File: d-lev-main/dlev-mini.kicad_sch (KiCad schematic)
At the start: 5 parts

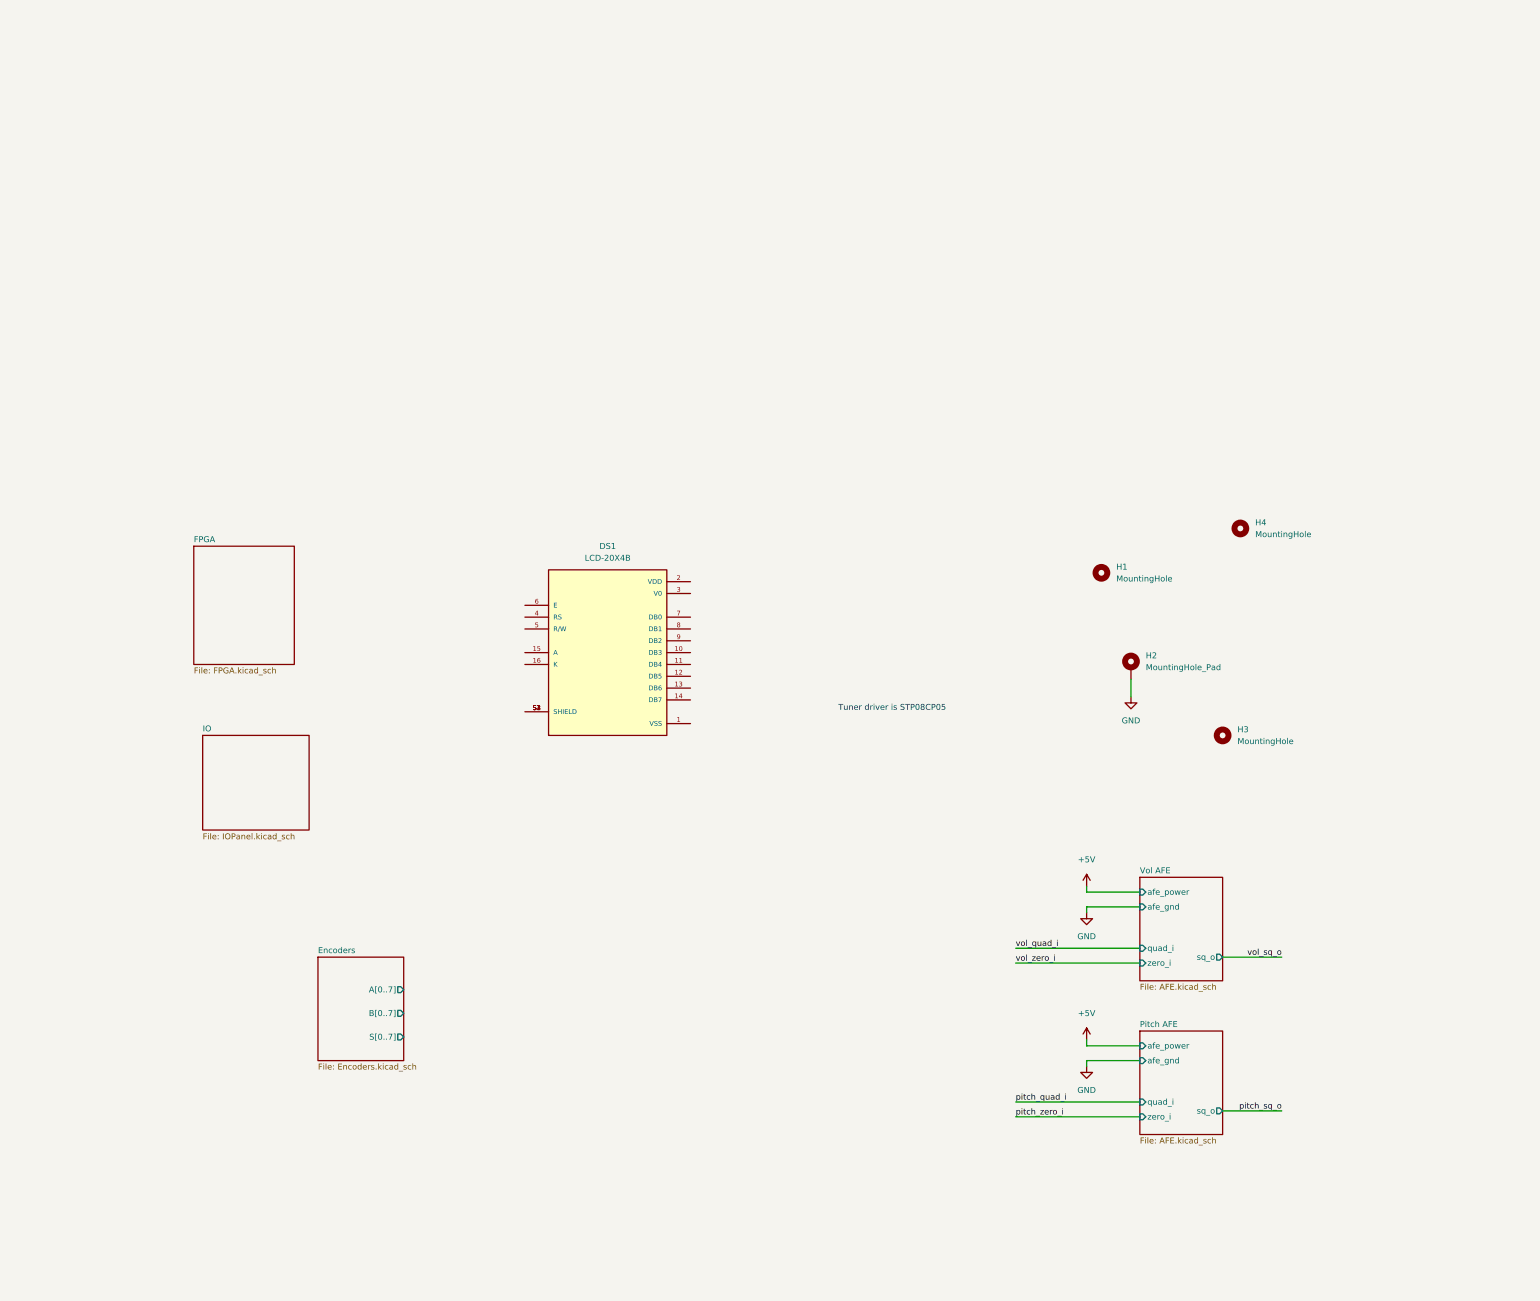
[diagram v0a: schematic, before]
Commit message: Add block diagram
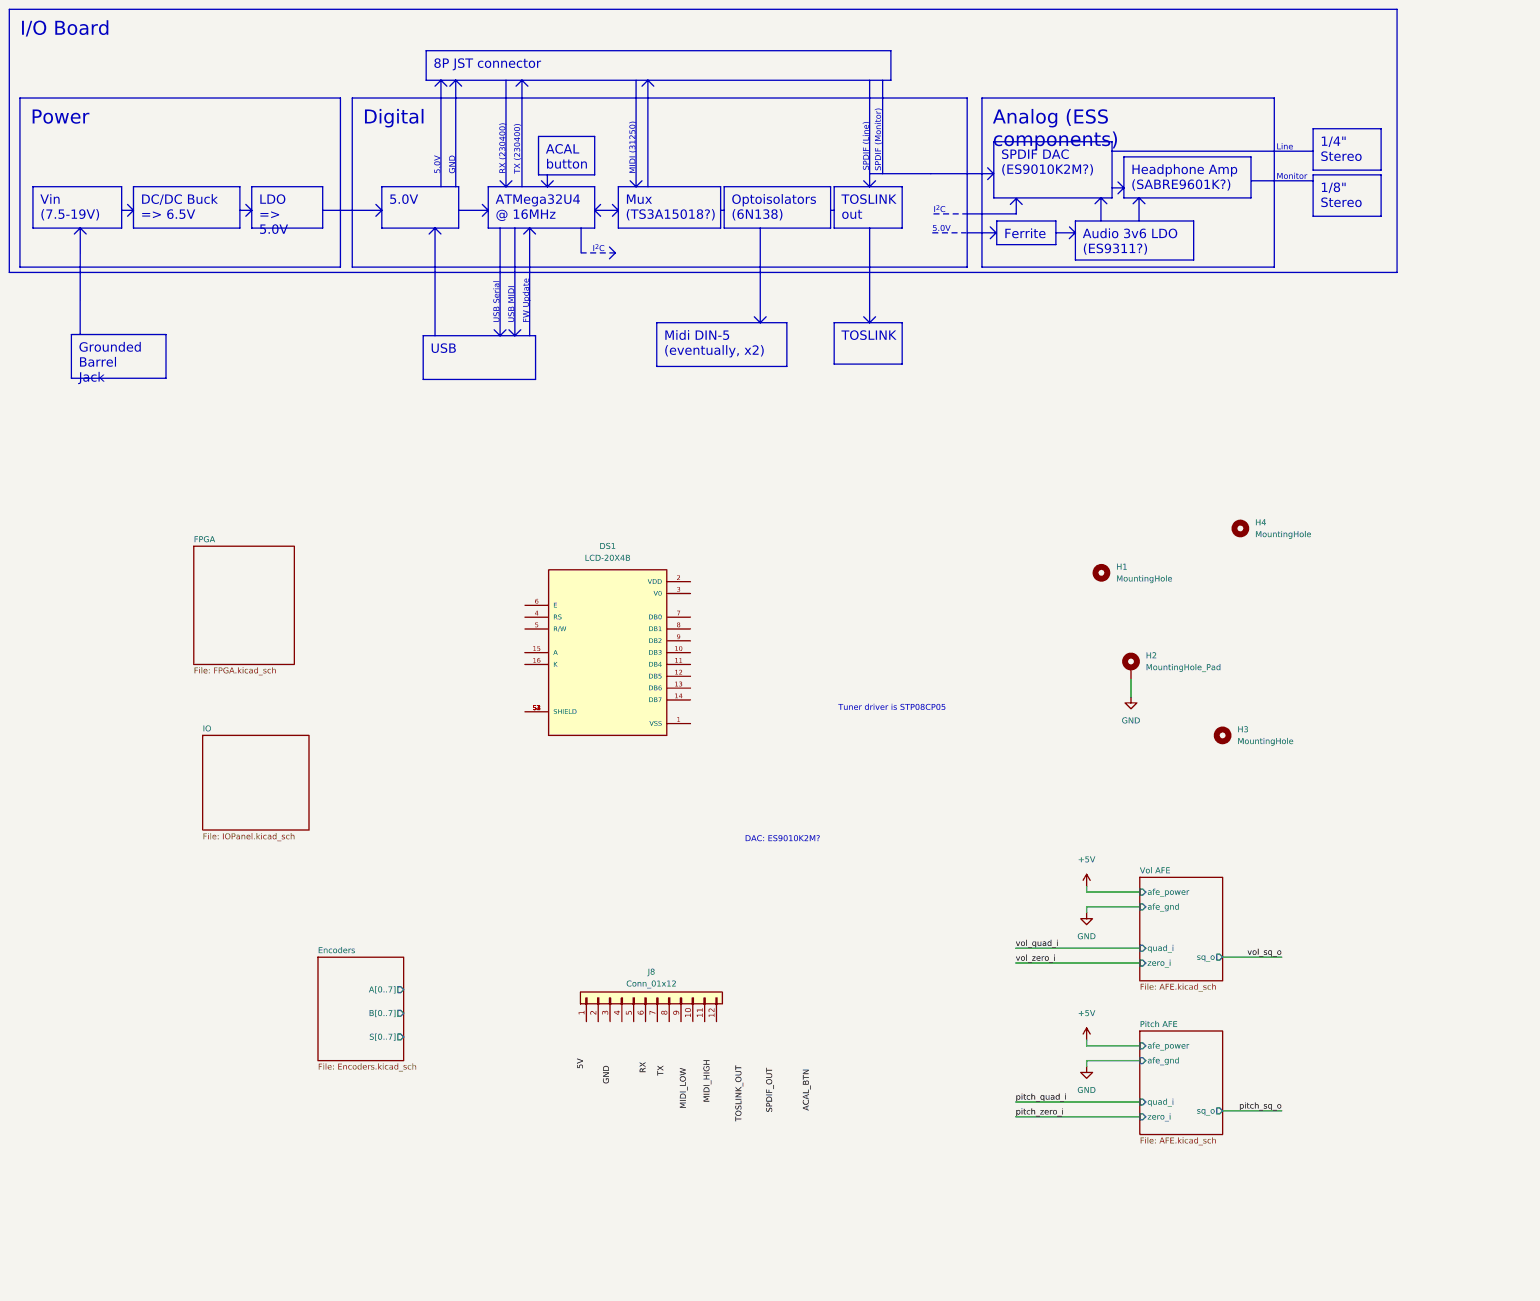
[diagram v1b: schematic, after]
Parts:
- added J8: Conn_01x12, symbol Connector_Generic:Conn_01x12
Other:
- note added: "5.0V"
- note added: "DAC: ES9010K2M?"
- note added: "FW Update"
- note added: "GND"
- note added: "I^{2}C"
- note added: "Line"
- note added: "MIDI (31250)"
- note added: "Monitor"
- note added: "RX (230400)"
- note added: "SPDIF (Line)"
- note added: "SPDIF (Monitor)"
- note added: "TX (230400)"
- note added: "USB MIDI"
- note added: "USB Serial"

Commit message: Many changes
Reorganized libraries to share between projects
Set up JLC 2- and 4- layer design rules
Finished copying over most of the schematic (excluding I/O board)
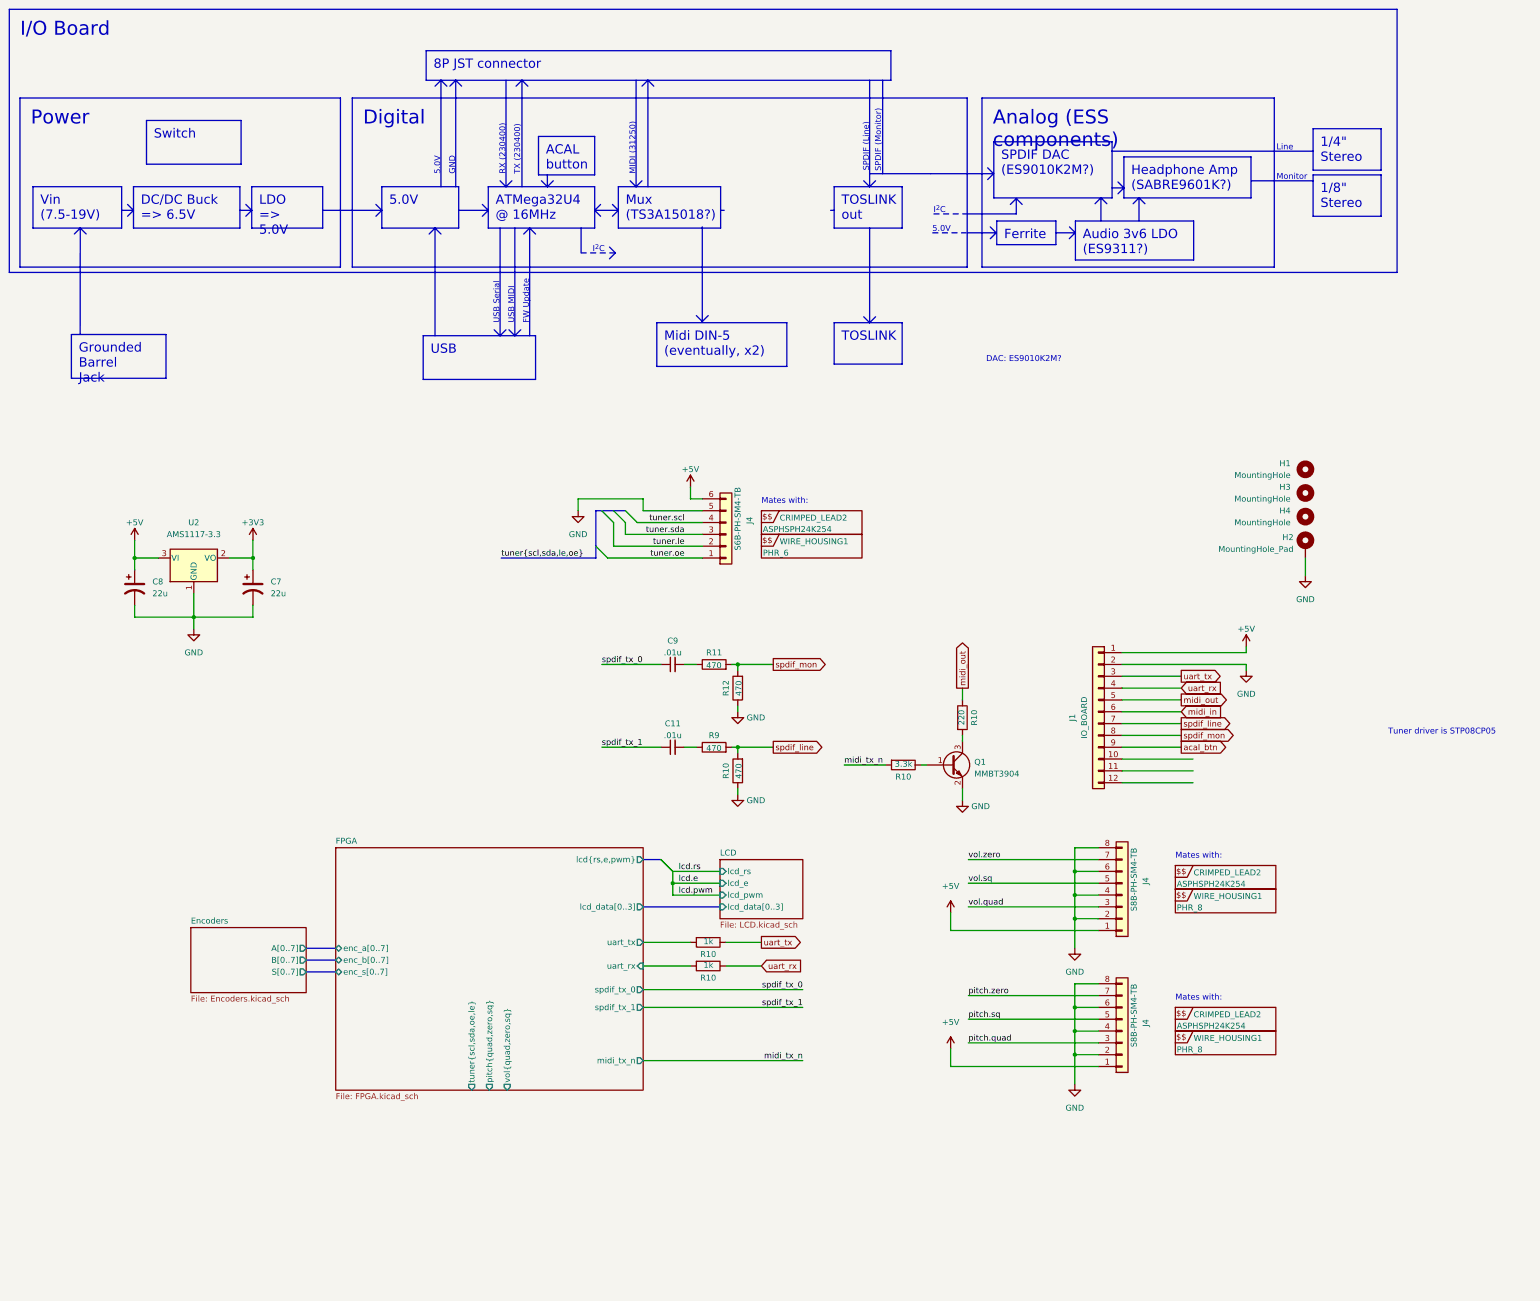
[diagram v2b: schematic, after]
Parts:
- removed DS1: LCD-20X4B, footprints:ERM2004-1, symbol LCD-20X4B:LCD-20X4B
- added C11, C9: .01u, symbol Device:C_Small
- added C7, C8: 22u, symbol Device:C_Polarized_US
- added CRIMPED_LEAD2 (x3): ASPHSPH24K254, symbol assorted:BOM_ITEM
- added J4 (x2): S8B-PH-SM4-TB, Connector_JST:JST_PH_S8B-PH-SM4-TB_1x08-1MP_P2.00mm_Horizontal, symbol Connector_Generic:Conn_01x08
- added J4: S6B-PH-SM4-TB, Connector_JST:JST_PH_S6B-PH-SM4-TB_1x06-1MP_P2.00mm_Horizontal, symbol Connector_Generic:Conn_01x06
- added Q1: MMBT3904, Package_TO_SOT_SMD:SOT-23, symbol Transistor_BJT:MMBT3904
- added R10: 220, symbol Device:R
- added R10, R11, R12, R9: 470, symbol Device:R
- added R10: 3.3k, symbol Device:R
- added R10 (x2): 1k, symbol Device:R
- added U2: AMS1117-3.3, Package_TO_SOT_SMD:SOT-223-3_TabPin2, symbol Regulator_Linear:AMS1117-3.3
- added WIRE_HOUSING1: PHR_6, symbol assorted:BOM_ITEM
- added WIRE_HOUSING1 (x2): PHR_8, symbol assorted:BOM_ITEM
- H3, H4: footprint (none) -> d-lev:SMTSO-M4
- J1: renamed from J8; value Conn_01x12 -> IO_BOARD
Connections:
- net +5V: now also J1.1 (Pin_1), C8.1, J4.1 (Pin_1), J4.1 (Pin_1), J4.6 (Pin_6), U2.3 (VI)
- net GND: now also J1.2 (Pin_2), C7.2, C8.2, J4.2 (Pin_2), J4.2 (Pin_2), J4.4 (Pin_4), J4.4 (Pin_4), J4.5 (Pin_5), J4.6 (Pin_6), J4.6 (Pin_6), J4.8 (Pin_8), J4.8 (Pin_8), Q1.2 (E), R10.1, R12.1, U2.1 (GND)
- net uart_tx: now reaches J1.3 (Pin_3)
- net uart_tx: now also R10.1
- net uart_rx: now reaches J1.4 (Pin_4)
- net uart_rx: now also R10.1
- net midi_out: now reaches J1.5 (Pin_5)
- net midi_out: now also R10.1
- net midi_in: now reaches J1.6 (Pin_6)
- net spdif_line: now reaches J1.7 (Pin_7)
- net spdif_line: now also R10.2, R9.2
- net spdif_mon: now reaches J1.8 (Pin_8)
- net spdif_mon: now also R11.2, R12.2
- net acal_btn: now reaches J1.9 (Pin_9)
- new net: Q1.3 (C), R10.2
- new net: C9.2, R11.1
- new net: Q1.1 (B), R10.1
- new net: C11.2, R9.1
- new net +3V3: C7.1, U2.2 (VO)
- new net FPGA/uart_rx: R10.2
- new net FPGA/uart_tx: R10.2
- new net midi_tx_n: R10.2
- new net pitch.quad: J4.3 (Pin_3)
- new net pitch.sq: J4.5 (Pin_5)
- new net pitch.zero: J4.7 (Pin_7)
- new net spdif_tx_0: C9.1
- new net spdif_tx_1: C11.1
- new net tuner.le: J4.2 (Pin_2)
- new net tuner.oe: J4.1 (Pin_1)
- new net tuner.scl: J4.4 (Pin_4)
- new net tuner.sda: J4.3 (Pin_3)
- new net vol.quad: J4.3 (Pin_3)
- new net vol.sq: J4.5 (Pin_5)
- new net vol.zero: J4.7 (Pin_7)
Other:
- removed sheet IO
- removed sheet Pitch AFE
- removed sheet Vol AFE
- added sheet LCD (LCD.kicad_sch)
- sheet FPGA ports: added enc_a[0..7], enc_b[0..7], enc_s[0..7], lcd_data[0..3], lcd{rs,e,pwm}, midi_tx_n, pitch{quad,zero,sq}, spdif_tx_0, spdif_tx_1, tuner{scl,sda,oe,le}, uart_rx, uart_tx, vol{quad,zero,sq}; removed none
- note added: "Mates with:"
- moved on the sheet: H1, H2, H3, H4, J1

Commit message: schematic + wiring for avr
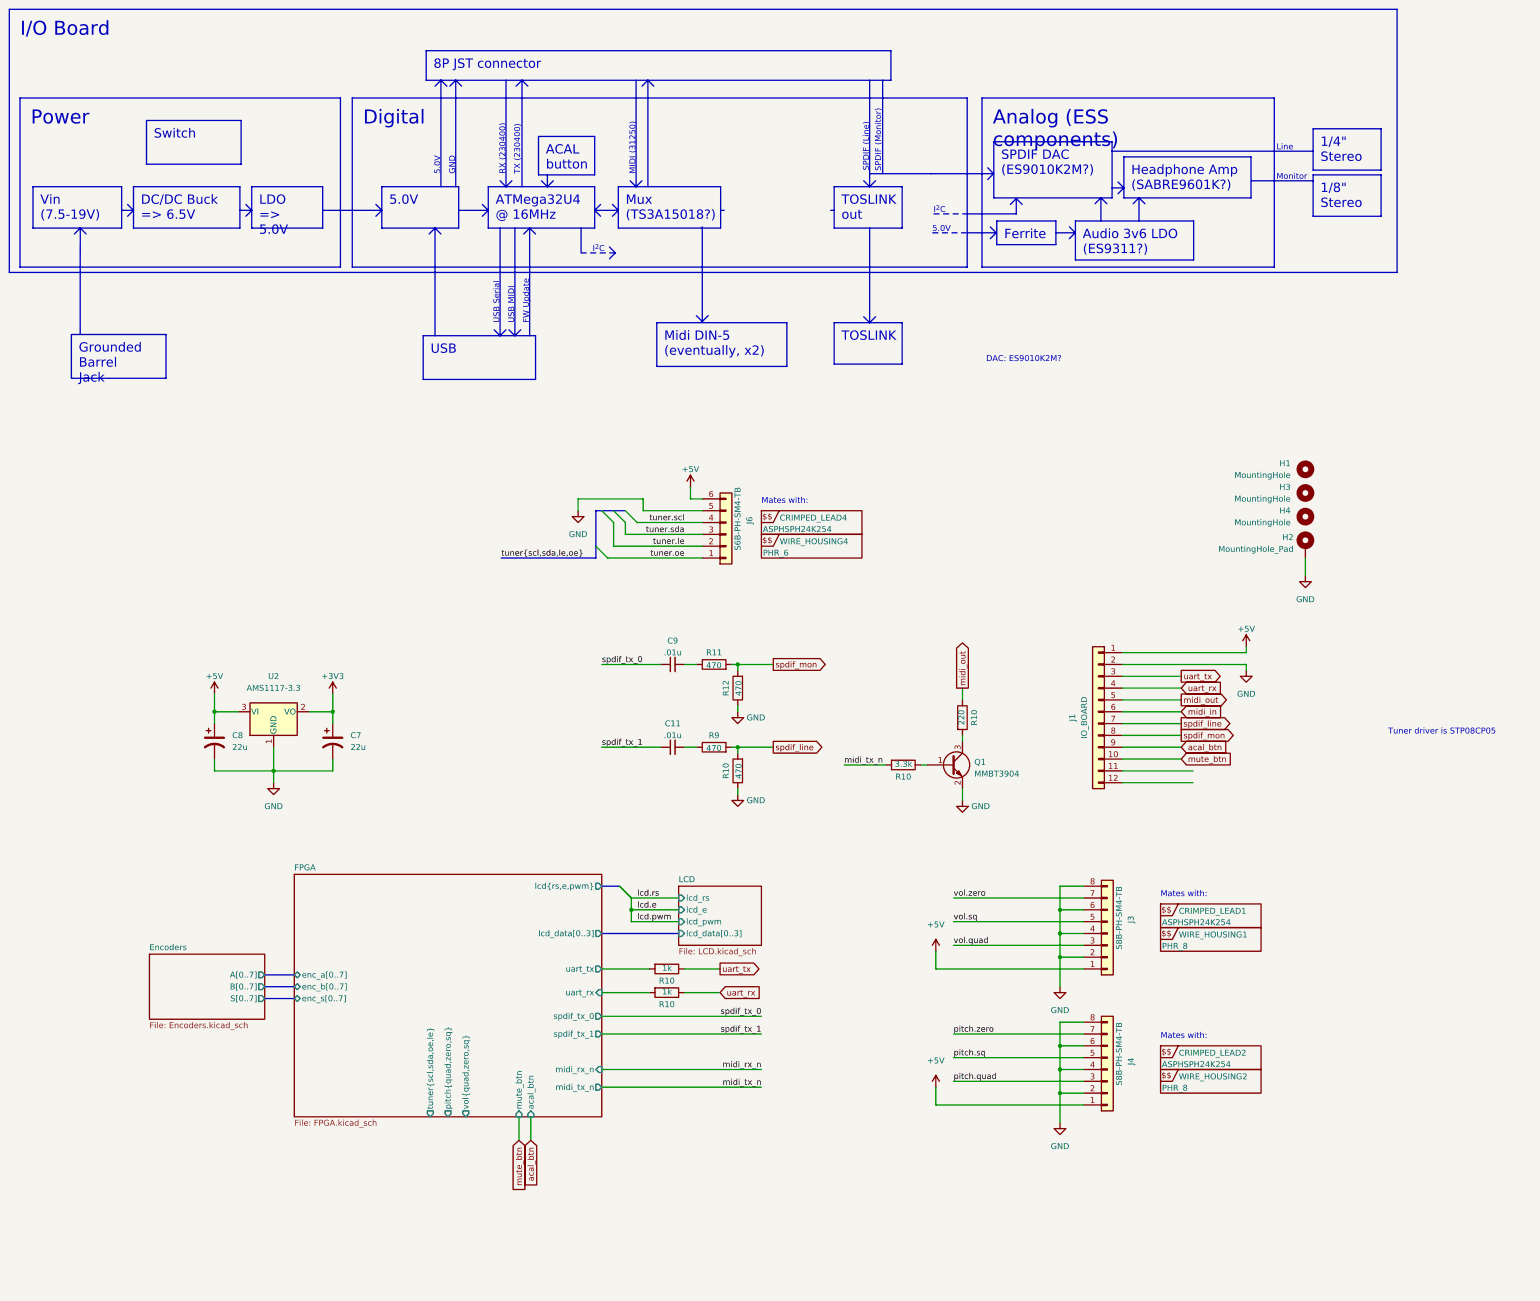
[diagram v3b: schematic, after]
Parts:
- renumbered CRIMPED_LEAD2 to CRIMPED_LEAD1, CRIMPED_LEAD2 to CRIMPED_LEAD4, J4 to J3, J4 to J6, WIRE_HOUSING1 to WIRE_HOUSING2, WIRE_HOUSING1 to WIRE_HOUSING4
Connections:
- net mute_btn: now reaches J1.10 (Pin_10)
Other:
- sheet FPGA ports: added acal_btn, midi_rx_n, mute_btn; removed none
- moved on the sheet: C7, C8, CRIMPED_LEAD1, CRIMPED_LEAD2, J3, J4, R10, U2, WIRE_HOUSING1, WIRE_HOUSING2
